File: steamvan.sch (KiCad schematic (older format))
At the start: 24 parts, among them J1 Conn_01x05_Male, Q1 FMMT493TA, SW1 SW_Push, U1 STM32F303CBTx, U2 TLV70233_SOT23-5, U3 NUF2221W1T2G, Y1 8MHz

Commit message: Add: new minivan layouts, and start switching to MX/Alps hybrid footprints
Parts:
- C1, C10, C11, C2, C3, C4, C5, C6, C7, C8, C9: footprint (none) -> Capacitor_SMD:C_0603_1608Metric
- F1: footprint (none) -> Resistor_SMD:R_0805_2012Metric
- J1: footprint (none) -> Connector_PinHeader_2.54mm:PinHeader_1x05_P2.54mm_Vertical
- RC1, RC6, RC7, RC8: footprint (none) -> Resistor_SMD:R_0603_1608Metric
- SW1: footprint (none) -> Button_Switch_SMD:SW_SPST_TL3342
- U3: footprint SOT-363 -> digikey-footprints:SOT-363
- USB1: footprint (none) -> Type-C:HRO-TYPE-C-31-M-12-Assembly
- Y1: footprint (none) -> Crystal:Crystal_SMD_5032-4Pin_5.0x3.2mm
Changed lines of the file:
@@
 F 0 "Y1" H 4526 4081 50  0000 L CNN
 F 1 "8MHz" H 4526 3990 50  0000 L CNN
-F 2 "" H 4335 4035 50  0001 C CNN
+F 2 "Crystal:Crystal_SMD_5032-4Pin_5.0x3.2mm" H 4335 4035 50  0001 C CNN
 F 3 "~" H 4335 4035 50  0001 C CNN
 	1    4335 4035
@@
 F 0 "USB1" H 1266 4307 60  0000 C CNN
 F 1 "HRO-TYPE-C-31-M-12" H 1266 4201 60  0000 C CNN
-F 2 "" H 1435 3510 60  0001 C CNN
+F 2 "Type-C:HRO-TYPE-C-31-M-12-Assembly" H 1435 3510 60  0001 C CNN
 F 3 "" H 1435 3510 60  0001 C CNN
 	1    1435 3510
@@
 F 0 "C1" H 4010 4291 50  0000 L CNN
 F 1 "30p" H 4010 4200 50  0000 L CNN
-F 2 "" H 3933 4095 50  0001 C CNN
+F 2 "Capacitor_SMD:C_0603_1608Metric" H 3933 4095 50  0001 C CNN
 F 3 "~" H 3895 4245 50  0001 C CNN
 	1    3895 4245
@@
 F 0 "C2" H 4940 4296 50  0000 L CNN
 F 1 "30p" H 4940 4205 50  0000 L CNN
-F 2 "" H 4863 4100 50  0001 C CNN
+F 2 "Capacitor_SMD:C_0603_1608Metric" H 4863 4100 50  0001 C CNN
 F 3 "~" H 4825 4250 50  0001 C CNN
 	1    4825 4250
@@
 F 0 "C10" H 2285 6201 50  0000 L CNN
 F 1 "1u" H 2285 6110 50  0000 L CNN
-F 2 "" H 2208 6005 50  0001 C CNN
+F 2 "Capacitor_SMD:C_0603_1608Metric" H 2208 6005 50  0001 C CNN
 F 3 "~" H 2170 6155 50  0001 C CNN
 	1    2170 6155
@@
 F 0 "C11" H 3145 6201 50  0000 L CNN
 F 1 "1u" H 3145 6110 50  0000 L CNN
-F 2 "" H 3068 6005 50  0001 C CNN
+F 2 "Capacitor_SMD:C_0603_1608Metric" H 3068 6005 50  0001 C CNN
 F 3 "~" H 3030 6155 50  0001 C CNN
 	1    3030 6155
@@
 F 0 "U3" H 4675 2815 50  0001 L BNN
 F 1 "NUF2221W1T2G" H 4675 2815 50  0001 L BNN
-F 2 "SOT-363" H 4675 2815 50  0001 L BNN
+F 2 "digikey-footprints:SOT-363" H 4675 2815 50  0001 L BNN
 F 3 "Good" H 4675 2815 50  0001 L BNN
 F 4 "SOT-363 ON Semiconductor" H 4675 2815 50  0001 L BNN "Field4"
@@
 F 0 "RC1" V 4798 1265 50  0000 C CNN
 F 1 "470" V 4889 1265 50  0000 C CNN
-F 2 "" V 4935 1265 50  0001 C CNN
+F 2 "Resistor_SMD:R_0603_1608Metric" V 4935 1265 50  0001 C CNN
 F 3 "~" H 5005 1265 50  0001 C CNN
 	1    5005 1265
@@
 F 0 "C6" H 1175 1251 50  0000 L CNN
 F 1 "1u" H 1175 1160 50  0000 L CNN
-F 2 "" H 1098 1055 50  0001 C CNN
+F 2 "Capacitor_SMD:C_0603_1608Metric" H 1098 1055 50  0001 C CNN
 F 3 "~" H 1060 1205 50  0001 C CNN
 	1    1060 1205
@@
 F 0 "C7" H 1550 1251 50  0000 L CNN
 F 1 "10n" H 1550 1160 50  0000 L CNN
-F 2 "" H 1473 1055 50  0001 C CNN
+F 2 "Capacitor_SMD:C_0603_1608Metric" H 1473 1055 50  0001 C CNN
 F 3 "~" H 1435 1205 50  0001 C CNN
 	1    1435 1205
@@
 F 0 "C5" H 2070 1251 50  0000 L CNN
 F 1 "4.7u" H 2070 1160 50  0000 L CNN
-F 2 "" H 1993 1055 50  0001 C CNN
+F 2 "Capacitor_SMD:C_0603_1608Metric" H 1993 1055 50  0001 C CNN
 F 3 "~" H 1955 1205 50  0001 C CNN
 	1    1955 1205
@@
 F 0 "C4" H 2455 1246 50  0000 L CNN
 F 1 "100n" H 2455 1155 50  0000 L CNN
-F 2 "" H 2378 1050 50  0001 C CNN
+F 2 "Capacitor_SMD:C_0603_1608Metric" H 2378 1050 50  0001 C CNN
 F 3 "~" H 2340 1200 50  0001 C CNN
 	1    2340 1200
@@
 F 0 "C3" H 2890 1246 50  0000 L CNN
 F 1 "100n" H 2890 1155 50  0000 L CNN
-F 2 "" H 2813 1050 50  0001 C CNN
+F 2 "Capacitor_SMD:C_0603_1608Metric" H 2813 1050 50  0001 C CNN
 F 3 "~" H 2775 1200 50  0001 C CNN
 	1    2775 1200
@@
 F 0 "C8" H 3305 1246 50  0000 L CNN
 F 1 "100n" H 3305 1155 50  0000 L CNN
-F 2 "" H 3228 1050 50  0001 C CNN
+F 2 "Capacitor_SMD:C_0603_1608Metric" H 3228 1050 50  0001 C CNN
 F 3 "~" H 3190 1200 50  0001 C CNN
 	1    3190 1200
@@
 F 0 "F1" V 1730 3060 50  0000 C CNN
 F 1 "500mA" V 1821 3060 50  0000 C CNN
-F 2 "" H 2005 2860 50  0001 L CNN
+F 2 "Resistor_SMD:R_0805_2012Metric" H 2005 2860 50  0001 L CNN
 F 3 "~" H 1955 3060 50  0001 C CNN
 	1    1955 3060
@@
 F 0 "RC6" V 2183 3260 50  0000 C CNN
 F 1 "5.1k" V 2274 3260 50  0000 C CNN
-F 2 "" V 2320 3260 50  0001 C CNN
+F 2 "Resistor_SMD:R_0603_1608Metric" V 2320 3260 50  0001 C CNN
 F 3 "~" H 2390 3260 50  0001 C CNN
 	1    2390 3260
@@
 F 0 "RC7" V 2183 3860 50  0000 C CNN
 F 1 "5.1k" V 2274 3860 50  0000 C CNN
-F 2 "" V 2320 3860 50  0001 C CNN
+F 2 "Resistor_SMD:R_0603_1608Metric" V 2320 3860 50  0001 C CNN
 F 3 "~" H 2390 3860 50  0001 C CNN
 	1    2390 3860
@@
 F 0 "J1" H 9861 1988 50  0000 C CNN
 F 1 "Conn_01x05_Male" H 9861 1897 50  0000 C CNN
-F 2 "" H 9755 1610 50  0001 C CNN
+F 2 "Connector_PinHeader_2.54mm:PinHeader_1x05_P2.54mm_Vertical" H 9755 1610 50  0001 C CNN
 F 3 "~" H 9755 1610 50  0001 C CNN
 	1    9755 1610
@@
 F 0 "C9" H 7370 2056 50  0000 L CNN
 F 1 "100n" H 7370 1965 50  0000 L CNN
-F 2 "" H 7293 1860 50  0001 C CNN
+F 2 "Capacitor_SMD:C_0603_1608Metric" H 7293 1860 50  0001 C CNN
 F 3 "~" H 7255 2010 50  0001 C CNN
 	1    7255 2010
@@
 F 0 "SW1" H 6465 2725 50  0000 C CNN
 F 1 "SW_Push" H 6465 2634 50  0000 C CNN
-F 2 "" H 6465 2640 50  0001 C CNN
+F 2 "Button_Switch_SMD:SW_SPST_TL3342" H 6465 2640 50  0001 C CNN
 F 3 "" H 6465 2640 50  0001 C CNN
 	1    6465 2440
@@
 F 0 "RC8" H 6820 2731 50  0000 L CNN
 F 1 "10k" H 6820 2640 50  0000 L CNN
-F 2 "" V 6680 2685 50  0001 C CNN
+F 2 "Resistor_SMD:R_0603_1608Metric" V 6680 2685 50  0001 C CNN
 F 3 "~" H 6750 2685 50  0001 C CNN
 	1    6750 2685

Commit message: Update: Work on routing
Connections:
- net COL6 is gone; now on net COL1: U1.30 (PA9)
- net COL0: now also U1.31 (PA10); no longer U1.12 (PA2)
- no-connect marks 16 -> 15
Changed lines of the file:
@@
 Wire Wire Line
 	9125 4840 9005 4840
-Text GLabel 9135 3540 2    50   Input ~ 0
+Text GLabel 9135 4340 2    50   Input ~ 0
 COL0
-Wire Wire Line
-	9135 3540 9005 3540
 Text GLabel 9135 3640 2    50   Input ~ 0
 COL1
@@
 COL5
 Text GLabel 9135 4240 2    50   Input ~ 0
-COL6
+COL1
 Wire Wire Line
 	9005 4140 9135 4140
@@
 NoConn ~ 9005 3740
 NoConn ~ 9005 3840
-NoConn ~ 9005 4340
 NoConn ~ 7705 4640
 NoConn ~ 7705 4540
@@
 Wire Wire Line
 	2215 2865 2215 2825
+Wire Wire Line
+	9005 4340 9135 4340
 $EndSCHEMATC

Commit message: Update: Work on routing
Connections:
- net COL10: now also U1.39 (PB3); no longer U1.3 (PC14)
- net COL11: now also U1.38 (PA15); no longer U1.4 (PC15)
- net COL2: now also U1.29 (PA8); no longer U1.16 (PA6)
- net COL3: now also U1.28 (PB15); no longer U1.27 (PB14)
- net COL4: now also U1.27 (PB14); no longer U1.28 (PB15)
- net COL5: now also U1.16 (PA6); no longer U1.29 (PA8)
- net COL7: now also U1.42 (PB6)
- net COL8: now also U1.41 (PB5); no longer U1.39 (PB3)
- net ROW3: now also U1.4 (PC15); no longer U1.38 (PA15)
- no-connect marks 15 -> 14
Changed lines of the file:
@@
 	7485 3540 7705 3540
 Text GLabel 9125 4840 2    50   Input ~ 0
-ROW3
+COL11
 Wire Wire Line
 	9125 4840 9005 4840
@@
 	9135 3640 9005 3640
 Text GLabel 9135 3940 2    50   Input ~ 0
-COL2
+COL5
 Wire Wire Line
 	9005 3940 9135 3940
 Text GLabel 7545 4740 0    50   Input ~ 0
+COL4
+Text GLabel 7545 4840 0    50   Input ~ 0
 COL3
-Text GLabel 7545 4840 0    50   Input ~ 0
-COL4
 Wire Wire Line
 	7545 4840 7705 4840
@@
 	7545 4740 7705 4740
 Text GLabel 9135 4140 2    50   Input ~ 0
-COL5
+COL2
 Text GLabel 9135 4240 2    50   Input ~ 0
 COL1
@@
 	9005 4040 9130 4040
 Text GLabel 7485 3640 0    50   Input ~ 0
-COL8
-Text GLabel 7485 3740 0    50   Input ~ 0
-COL9
+COL10
 Wire Wire Line
 	7485 3640 7705 3640
-Wire Wire Line
-	7485 3740 7705 3740
-Text GLabel 7485 3040 0    50   Input ~ 0
-COL10
 Text GLabel 7485 3140 0    50   Input ~ 0
-COL11
-Wire Wire Line
-	7485 3040 7705 3040
+ROW3
 Wire Wire Line
 	7485 3140 7705 3140
@@
 NoConn ~ 7705 4240
 NoConn ~ 7705 4040
-NoConn ~ 7705 3940
-NoConn ~ 7705 3840
 $Comp
 L power:PWR_FLAG #FLG0101
@@
 Wire Wire Line
 	9005 4340 9135 4340
+Text GLabel 7485 3840 0    50   Input ~ 0
+COL8
+Wire Wire Line
+	7485 3840 7705 3840
+NoConn ~ 7705 3040
+Text GLabel 7485 3940 0    50   Input ~ 0
+COL7
+Wire Wire Line
+	7485 3740 7705 3740
+Text GLabel 7485 3740 0    50   Input ~ 0
+COL9
+Wire Wire Line
+	7485 3940 7705 3940
 $EndSCHEMATC

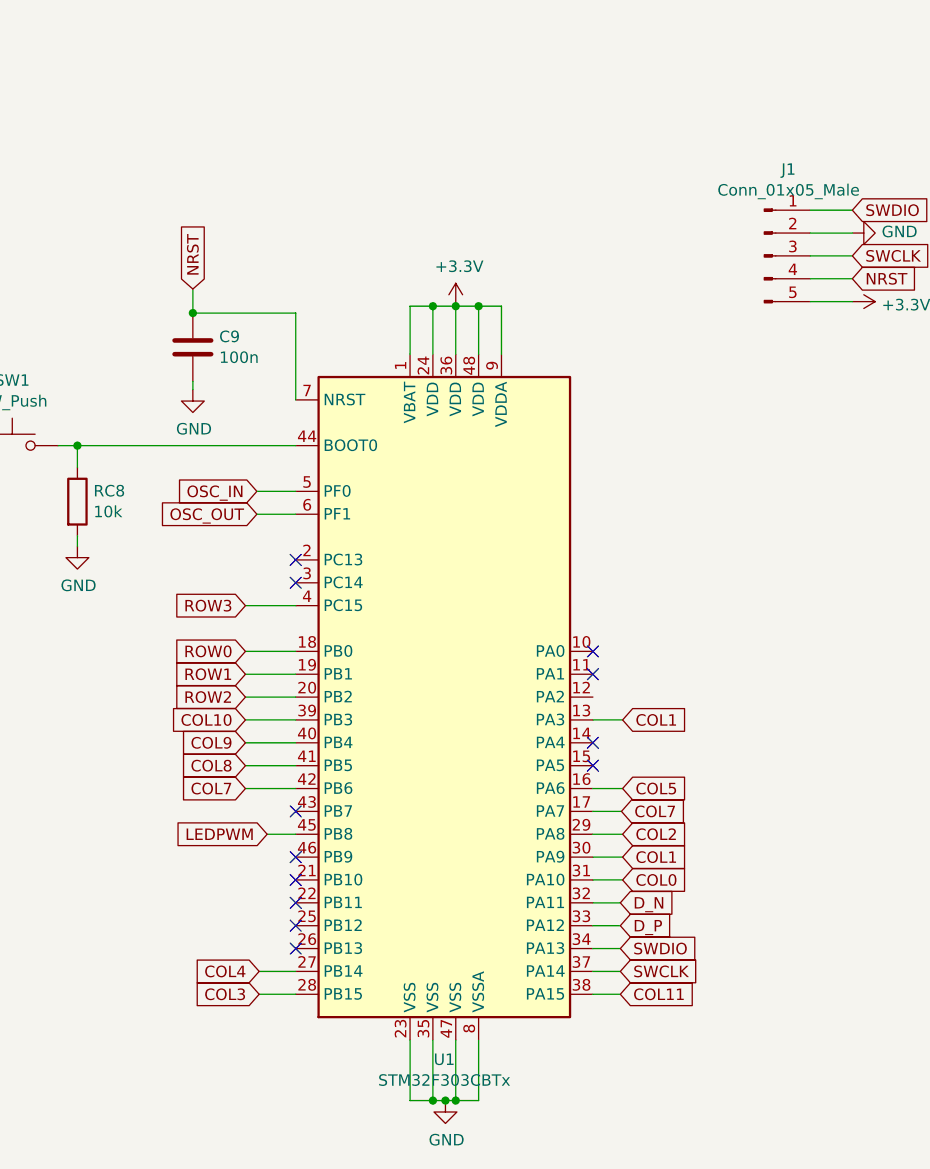
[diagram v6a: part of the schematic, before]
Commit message: Update: Add schematic components for RGB underglow, and work on routing
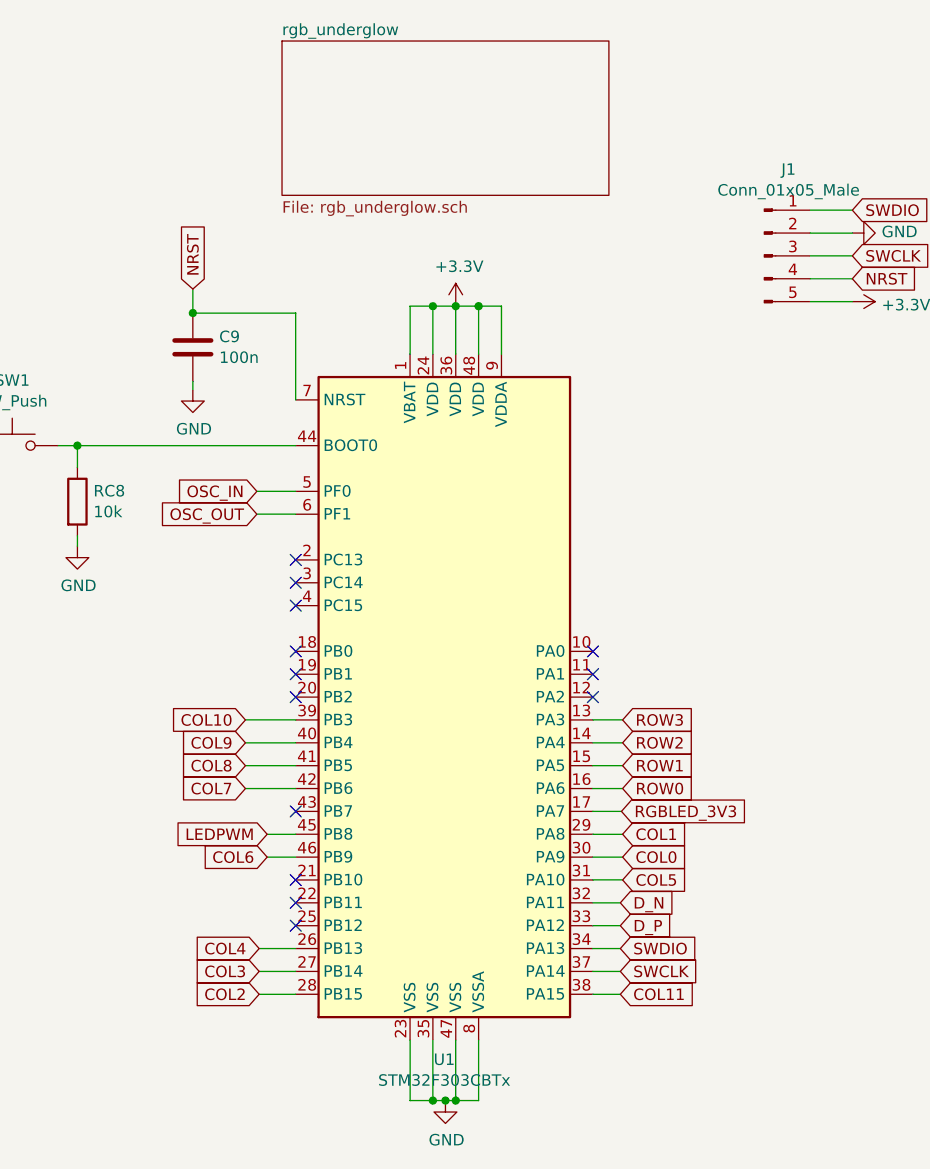
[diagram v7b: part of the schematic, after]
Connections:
- net COL0: now also U1.30 (PA9); no longer U1.31 (PA10)
- net COL1: now also U1.29 (PA8); no longer U1.13 (PA3), U1.30 (PA9)
- net COL2: now also U1.28 (PB15); no longer U1.29 (PA8)
- net COL3: now also U1.27 (PB14); no longer U1.28 (PB15)
- net COL4: now also U1.26 (PB13); no longer U1.27 (PB14)
- net COL5: now also U1.31 (PA10); no longer U1.16 (PA6)
- net COL7: no longer U1.17 (PA7)
- net ROW0: now also U1.16 (PA6); no longer U1.18 (PB0)
- net ROW1: now also U1.15 (PA5); no longer U1.19 (PB1)
- net ROW2: now also U1.14 (PA4); no longer U1.20 (PB2)
- net ROW3: now also U1.13 (PA3); no longer U1.4 (PC15)
- net COL6: now reaches U1.46 (PB9)
- new net RGBLED_3V3: U1.17 (PA7)
- no-connect marks 14 -> 15
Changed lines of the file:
@@
 $Descr A4 11693 8268
 encoding utf-8
-Sheet 1 2
+Sheet 1 3
 Title ""
 Date ""
@@
 F1 "matrix.sch" 50
 $EndSheet
-Text GLabel 7485 3340 0    50   Input ~ 0
-ROW0
-Text GLabel 7485 3440 0    50   Input ~ 0
-ROW1
-Text GLabel 7485 3540 0    50   Input ~ 0
-ROW2
-Wire Wire Line
-	7485 3340 7705 3340
-Wire Wire Line
-	7705 3440 7485 3440
-Wire Wire Line
-	7485 3540 7705 3540
 Text GLabel 9125 4840 2    50   Input ~ 0
 COL11
@@
 	9125 4840 9005 4840
 Text GLabel 9135 4340 2    50   Input ~ 0
-COL0
+COL5
 Text GLabel 9135 3640 2    50   Input ~ 0
-COL1
+ROW3
 Wire Wire Line
 	9135 3640 9005 3640
 Text GLabel 9135 3940 2    50   Input ~ 0
-COL5
+ROW0
 Wire Wire Line
 	9005 3940 9135 3940
 Text GLabel 7545 4740 0    50   Input ~ 0
-COL4
+COL3
 Text GLabel 7545 4840 0    50   Input ~ 0
-COL3
+COL2
 Wire Wire Line
 	7545 4840 7705 4840
@@
 	7545 4740 7705 4740
 Text GLabel 9135 4140 2    50   Input ~ 0
-COL2
+COL1
 Text GLabel 9135 4240 2    50   Input ~ 0
-COL1
+COL0
 Wire Wire Line
 	9005 4140 9135 4140
@@
 	9005 4240 9135 4240
 Text GLabel 9130 4040 2    50   Input ~ 0
-COL7
+RGBLED_3V3
 Wire Wire Line
 	9005 4040 9130 4040
@@
 Wire Wire Line
 	7485 3640 7705 3640
-Text GLabel 7485 3140 0    50   Input ~ 0
-ROW3
-Wire Wire Line
-	7485 3140 7705 3140
 NoConn ~ 7705 2940
 NoConn ~ 9005 3340
 NoConn ~ 9005 3440
-NoConn ~ 9005 3740
-NoConn ~ 9005 3840
-NoConn ~ 7705 4640
 NoConn ~ 7705 4540
 NoConn ~ 7705 4440
 NoConn ~ 7705 4340
-NoConn ~ 7705 4240
 NoConn ~ 7705 4040
 $Comp
@@
 Wire Wire Line
 	7485 3940 7705 3940
+Text GLabel 7580 4240 0    50   Input ~ 0
+COL6
+Wire Wire Line
+	7580 4240 7705 4240
+Text GLabel 7545 4640 0    50   Input ~ 0
+COL4
+Wire Wire Line
+	7545 4640 7705 4640
+Text GLabel 9135 3840 2    50   Input ~ 0
+ROW1
+Text GLabel 9135 3740 2    50   Input ~ 0
+ROW2
+Wire Wire Line
+	9005 3740 9135 3740
+Wire Wire Line
+	9005 3840 9135 3840
+NoConn ~ 7705 3340
+NoConn ~ 7705 3440
+NoConn ~ 7705 3540
+NoConn ~ 9005 3540
+$Sheet
+S 7645 670  1430 675
+U 5C6FFEF2
+F0 "rgb_underglow" 50
+F1 "rgb_underglow.sch" 50
+$EndSheet
+NoConn ~ 7705 3140
 $EndSCHEMATC

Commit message: Add: LCSC part numbers to schematic
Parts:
- C1, C2: LCSC PN (none) -> C22397
- C10, C11, C6: LCSC PN (none) -> C59782
- C3, C4, C8, C9: LCSC PN (none) -> C1590
- C5: LCSC PN (none) -> C19666
- C7: LCSC PN (none) -> C1589
- F1: LCSC PN (none) -> C66452
- Q1: LCSC PN (none) -> C47296
- RC6, RC7: LCSC PN (none) -> C14677
- RC8: LCSC PN (none) -> C98220
- SW1: LCSC PN (none) -> C92584
- U1: LCSC PN (none) -> C108516
- U2: LCSC PN (none) -> C26833
- U3: LCSC PN (none) -> C274624
- USB1: LCSC PN (none) -> C165948
- Y1: LCSC PN (none) -> C133333
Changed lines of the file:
@@
 F 2 "Package_QFP:LQFP-48_7x7mm_P0.5mm" H 7805 2140 50  0001 R CNN
 F 3 "http://www.st.com/st-web-ui/static/active/en/resource/technical/document/datasheet/DM00058181.pdf" H 8405 3540 50  0001 C CNN
+F 4 "C108516" H 8405 3540 50  0001 C CNN "LCSC PN"
 	1    8405 3540
 	1    0    0    -1
@@
 F 2 "Crystal:Crystal_SMD_5032-4Pin_5.0x3.2mm" H 4335 4035 50  0001 C CNN
 F 3 "~" H 4335 4035 50  0001 C CNN
+F 4 "C133333" H 4335 4035 50  0001 C CNN "LCSC PN"
 	1    4335 4035
 	1    0    0    -1
@@
 F 2 "Package_TO_SOT_SMD:SOT-23-5" H 2630 5925 50  0001 C CIN
 F 3 "http://www.ti.com/lit/ds/symlink/tlv702.pdf" H 2630 5650 50  0001 C CNN
+F 4 "C26833" H 2630 5600 50  0001 C CNN "LCSC PN"
 	1    2630 5600
 	1    0    0    -1
@@
 F 2 "Type-C:HRO-TYPE-C-31-M-12-Assembly" H 1435 3510 60  0001 C CNN
 F 3 "" H 1435 3510 60  0001 C CNN
+F 4 "C165948" H 1435 3510 50  0001 C CNN "LCSC PN"
 	1    1435 3510
 	1    0    0    -1
@@
 F 11 "Diodes Incorporated" H 5735 2365 60  0001 L CNN "Manufacturer"
 F 12 "Active" H 5735 2465 60  0001 L CNN "Status"
+F 13 "C47296" H 5535 1265 50  0001 C CNN "LCSC PN"
 	1    5535 1265
 	1    0    0    -1
@@
 F 2 "Capacitor_SMD:C_0603_1608Metric" H 3933 4095 50  0001 C CNN
 F 3 "~" H 3895 4245 50  0001 C CNN
+F 4 "C22397" H 3895 4245 50  0001 C CNN "LCSC PN"
 	1    3895 4245
 	1    0    0    -1
@@
 F 2 "Capacitor_SMD:C_0603_1608Metric" H 4863 4100 50  0001 C CNN
 F 3 "~" H 4825 4250 50  0001 C CNN
+F 4 "C22397" H 4825 4250 50  0001 C CNN "LCSC PN"
 	1    4825 4250
 	1    0    0    -1
@@
 F 2 "Capacitor_SMD:C_0603_1608Metric" H 2208 6005 50  0001 C CNN
 F 3 "~" H 2170 6155 50  0001 C CNN
+F 4 "C59782" H 2170 6155 50  0001 C CNN "LCSC PN"
 	1    2170 6155
 	1    0    0    -1
@@
 F 2 "Capacitor_SMD:C_0603_1608Metric" H 3068 6005 50  0001 C CNN
 F 3 "~" H 3030 6155 50  0001 C CNN
+F 4 "C59782" H 3030 6155 50  0001 C CNN "LCSC PN"
 	1    3030 6155
 	1    0    0    -1
@@
 F 7 "NUF2221W1T2G Series 8 V USB Upstream Terminator with ESD Protection - SC-88" H 4675 2815 50  0001 L BNN "Field7"
 F 8 "ON Semiconductor" H 4675 2815 50  0001 L BNN "Field8"
+F 9 "C274624" H 4675 2815 50  0001 C CNN "LCSC PN"
 	1    4675 2815
 	1    0    0    -1
@@
 F 2 "Capacitor_SMD:C_0603_1608Metric" H 1098 1055 50  0001 C CNN
 F 3 "~" H 1060 1205 50  0001 C CNN
+F 4 "C59782" H 1060 1205 50  0001 C CNN "LCSC PN"
 	1    1060 1205
 	1    0    0    -1
@@
 F 2 "Capacitor_SMD:C_0603_1608Metric" H 1473 1055 50  0001 C CNN
 F 3 "~" H 1435 1205 50  0001 C CNN
+F 4 "C1589" H 1435 1205 50  0001 C CNN "LCSC PN"
 	1    1435 1205
 	1    0    0    -1
@@
 F 2 "Capacitor_SMD:C_0603_1608Metric" H 1993 1055 50  0001 C CNN
 F 3 "~" H 1955 1205 50  0001 C CNN
+F 4 "C19666" H 1955 1205 50  0001 C CNN "LCSC PN"
 	1    1955 1205
 	1    0    0    -1
@@
 F 2 "Capacitor_SMD:C_0603_1608Metric" H 2378 1050 50  0001 C CNN
 F 3 "~" H 2340 1200 50  0001 C CNN
+F 4 "C1590" H 2340 1200 50  0001 C CNN "LCSC PN"
 	1    2340 1200
 	1    0    0    -1
@@
 F 2 "Capacitor_SMD:C_0603_1608Metric" H 2813 1050 50  0001 C CNN
 F 3 "~" H 2775 1200 50  0001 C CNN
+F 4 "C1590" H 2775 1200 50  0001 C CNN "LCSC PN"
 	1    2775 1200
 	1    0    0    -1
@@
 F 2 "Capacitor_SMD:C_0603_1608Metric" H 3228 1050 50  0001 C CNN
 F 3 "~" H 3190 1200 50  0001 C CNN
+F 4 "C1590" H 3190 1200 50  0001 C CNN "LCSC PN"
 	1    3190 1200
 	1    0    0    -1
@@
 F 2 "Resistor_SMD:R_0805_2012Metric" H 2005 2860 50  0001 L CNN
 F 3 "~" H 1955 3060 50  0001 C CNN
+F 4 "C66452" V 1955 3060 50  0001 C CNN "LCSC PN"
 	1    1955 3060
 	0    1    1    0
@@
 F 2 "Resistor_SMD:R_0603_1608Metric" V 2320 3260 50  0001 C CNN
 F 3 "~" H 2390 3260 50  0001 C CNN
+F 4 "C14677" V 2390 3260 50  0001 C CNN "LCSC PN"
 	1    2390 3260
 	0    1    1    0
@@
 F 2 "Resistor_SMD:R_0603_1608Metric" V 2320 3860 50  0001 C CNN
 F 3 "~" H 2390 3860 50  0001 C CNN
+F 4 "C14677" V 2390 3860 50  0001 C CNN "LCSC PN"
 	1    2390 3860
 	0    1    1    0
@@
 F 2 "Capacitor_SMD:C_0603_1608Metric" H 7293 1860 50  0001 C CNN
 F 3 "~" H 7255 2010 50  0001 C CNN
+F 4 "C1590" H 7255 2010 50  0001 C CNN "LCSC PN"
 	1    7255 2010
 	1    0    0    -1
@@
 F 2 "Button_Switch_SMD:SW_SPST_TL3342" H 6465 2640 50  0001 C CNN
 F 3 "" H 6465 2640 50  0001 C CNN
+F 4 "C92584" H 6465 2440 50  0001 C CNN "LCSC PN"
 	1    6465 2440
 	1    0    0    -1
@@
 F 2 "Resistor_SMD:R_0603_1608Metric" V 6680 2685 50  0001 C CNN
 F 3 "~" H 6750 2685 50  0001 C CNN
+F 4 "C98220" H 6750 2685 50  0001 C CNN "LCSC PN"
 	1    6750 2685
 	1    0    0    -1
